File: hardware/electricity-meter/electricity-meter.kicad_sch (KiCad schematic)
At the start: 70 parts, among them J1 Conn_01x20_Pin, J2 Conn_01x02_Pin, J3 FTDI breakout, J4 Conn_01x20_Pin, J5 ESB228110100Z, J6 Conn_01x08, J7 RJ45_Shielded, SW1 SW_DIP_x06, SW2 SW_Push, U1 DS3231M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

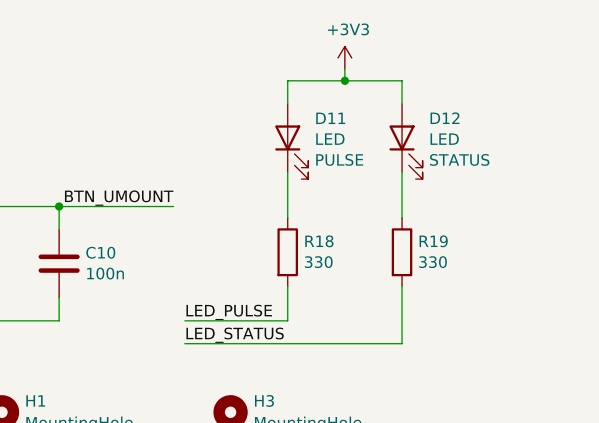
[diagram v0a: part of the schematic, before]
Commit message: Update hardware designs
* LED colors
* fix net ties excluded from ibom
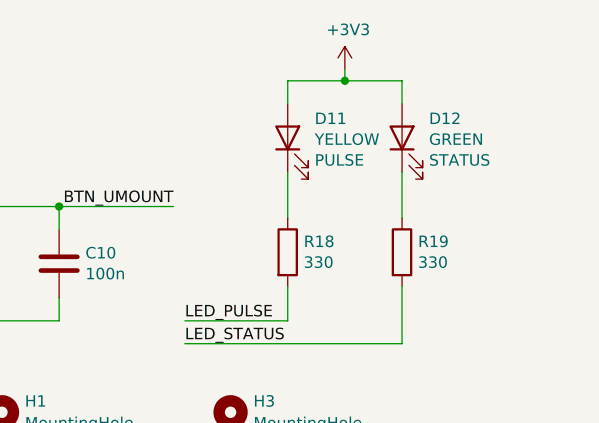
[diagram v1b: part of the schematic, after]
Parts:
- D11: value LED -> YELLOW
- D12: value LED -> GREEN
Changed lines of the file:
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@@
       (effects (font (size 1.27 1.27)) (justify right))
     )
-    (property "Value" "LED" (at 263.3472 25.5778 90)
+    (property "Value" "YELLOW" (at 263.3472 25.5778 90)
       (effects (font (size 1.27 1.27)) (justify right))
     )
@@
       (effects (font (size 1.27 1.27)) (justify right))
     )
-    (property "Value" "LED" (at 276.0472 25.5778 90)
+    (property "Value" "GREEN" (at 276.0472 25.5778 90)
       (effects (font (size 1.27 1.27)) (justify right))
     )

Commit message: Update documentation
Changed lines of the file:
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@@
           (reference "#PWR050") (unit 1)
-        )
-        (path "/ff3d9e8d-ce05-4912-9770-c80bf98d8dec/b212e67d-a601-4187-859b-ab25dade484d"
-          (reference "#PWR041") (unit 1)
         )
       )
@@
           (reference "JP3") (unit 1)
         )
-        (path "/ff3d9e8d-ce05-4912-9770-c80bf98d8dec/b212e67d-a601-4187-859b-ab25dade484d"
-          (reference "JP1") (unit 1)
-        )
       )
     )
@@
   )
   (symbol (lib_id "Memory_Flash:MX25L3233FM1") (at 222.25 144.78 0) (unit 1)
-    (in_bom yes) (on_board yes) (dnp no) (fields_autoplaced)
-    (property "Reference" "U5" (at 230.632 143.5679 0)
-      (effects (font (size 1.27 1.27)) (justify left))
-    )
-    (property "Value" "MX25L3233FM1" (at 230.632 145.9921 0)
-      (effects (font (size 1.27 1.27)) (justify left) hide)
+    (in_bom yes) (on_board yes) (dnp no)
+    (property "Reference" "U5" (at 224.79 157.48 0)
+      (effects (font (size 1.27 1.27)) (justify left))
+    )
+    (property "Value" "MX25L3233FM1" (at 224.79 160.02 0)
+      (effects (font (size 1.27 1.27)) (justify left))
     )
     (property "Footprint" "Package_SO:SOP-8_3.9x4.9mm_P1.27mm" (at 222.25 160.02 0)
@@
         (path "/ff3d9e8d-ce05-4912-9770-c80bf98d8dec"
           (reference "#PWR049") (unit 1)
-        )
-        (path "/ff3d9e8d-ce05-4912-9770-c80bf98d8dec/b212e67d-a601-4187-859b-ab25dade484d"
-          (reference "#PWR042") (unit 1)
         )
       )
@@
           (reference "#PWR046") (unit 1)
         )
-        (path "/ff3d9e8d-ce05-4912-9770-c80bf98d8dec/b212e67d-a601-4187-859b-ab25dade484d"
-          (reference "#PWR040") (unit 1)
-        )
       )
     )
@@
           (reference "J7") (unit 1)
         )
-        (path "/ff3d9e8d-ce05-4912-9770-c80bf98d8dec/b212e67d-a601-4187-859b-ab25dade484d"
-          (reference "J6") (unit 1)
-        )
-      )
+      )

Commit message: Add info about hardware mod
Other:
- note added: "mod: bridged over D9 to avoid insufficient input voltage for zigbee board (3v3 read 2.94V after AZ1117)"
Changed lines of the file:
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@@
+    (effects (font (size 1.27 1.27)) (justify left bottom))
+  )
+  (text "mod: bridged over D9 to avoid insufficient\ninput voltage for zigbee board (3v3 read 2.94V after AZ1117)"
+    (at 168.91 119.38 0)
     (effects (font (size 1.27 1.27)) (justify left bottom))
   )
